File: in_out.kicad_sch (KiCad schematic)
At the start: 22 parts, among them J2 Conn_01x10, J3 Micro_SD_Card_Det1, SW1 SW_Push, SW2 SW_Push, U6 DM-OLED096-636

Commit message: modify ios
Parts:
- removed R19, R20: R_Small, Resistor_SMD:R_0603_1608Metric, symbol Device:R_Small
- added Q3: NMOS, Package_TO_SOT_SMD:SOT-23, symbol Transistor_FET:Q_NMOS_GSD
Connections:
- net IO3_EXT is gone; now on net IO40_EXT: J2.6 (Pin_6), R16.2
- net IO46 is gone; now on net IO39_EXT: D5.1 (TVS1)
- net IO9_EXT is gone; now on net IO41_EXT: J2.5 (Pin_5), R17.2
- net +3V3: now also BZ1.1 (+), R23.1, R24.1, R25.1
- net BUZZER: now also Q3.1 (G); no longer BZ1.1 (+)
- net GND: now also Q3.2 (S); no longer BZ1.2 (-), D7.2 (BK), D7.4 (GK), D7.6 (RK)
- net RGB_B: now also D7.2 (BK); no longer R23.1
- net RGB_G: now also D7.4 (GK); no longer R24.1
- net RGB_R: now also D7.6 (RK); no longer R25.1
- net IO0: no longer names the net of D6.3 (TVS2)
- net IO0: no longer R15.1
- net IO0_EXT renamed IO39_EXT
- net IO14 renamed IO41_EXT
- net IO41_EXT: no longer R18.1
- net IO14_EXT renamed IO42_EXT
- net IO42_EXT: now also D5.6 (TVS4)
- net IO3: no longer names the net of D6.1 (TVS1)
- net IO3: no longer R16.1
- net IO38 renamed IO40_EXT
- net IO38_EXT: no longer names the net of J2.3 (Pin_3)
- net IO46_EXT: no longer names the net of J2.2 (Pin_2)
- net IO9 renamed IO41
- net IO41: no longer D5.6 (TVS4)
- new net: BZ1.2 (-), Q3.3 (D)
- new net IO39: R15.1
- new net IO40: R16.1
- new net IO42: R18.1
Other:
- moved on the sheet: BZ1, D7, R23, R24, R25

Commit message: update pcb and schematic
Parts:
- removed J2: Conn_01x10, Connector_PinSocket_2.54mm:PinSocket_1x10_P2.54mm_Horizontal, symbol Connector_Generic:Conn_01x10
- added J2: Conn_01x08, Connector_PinSocket_2.54mm:PinSocket_1x08_P2.54mm_Horizontal, symbol Connector_Generic:Conn_01x08
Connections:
- net +3V3: now also J2.1 (Pin_1)
- net GND: now also J2.8 (Pin_8)
- net IO39_EXT: now also J2.5 (Pin_5)
- net IO40_EXT: now also J2.4 (Pin_4)
- net IO41_EXT: now also J2.3 (Pin_3)
- net IO42_EXT: now also J2.2 (Pin_2)
- net RXD0_EXT: now also J2.7 (Pin_7)
- net TXD0_EXT: now also J2.6 (Pin_6)
- no-connect marks 0 -> 2
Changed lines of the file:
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@@
 		(color 0 0 0 0)
 	)
+	(no_connect
+		(at 125.73 113.03)
+	)
+	(no_connect
+		(at 128.27 113.03)
+	)
 	(wire
 		(pts
@@
 	(wire
 		(pts
-			(xy 128.27 110.49) (xy 128.27 113.03)
-		)
-		(stroke
-			(width 0)
-			(type default)
-		)
-	)
-	(wire
-		(pts
 			(xy 165.1 64.77) (xy 165.1 60.96)
 		)
@@
 	(wire
 		(pts
-			(xy 68.58 127) (xy 81.28 127)
+			(xy 67.31 123.19) (xy 80.01 123.19)
 		)
 		(stroke
@@
 	(wire
 		(pts
-			(xy 80.01 133.35) (xy 80.01 132.08)
+			(xy 78.74 129.54) (xy 78.74 128.27)
 		)
 		(stroke
@@
 	(wire
 		(pts
-			(xy 68.58 121.92) (xy 81.28 121.92)
+			(xy 67.31 118.11) (xy 80.01 118.11)
 		)
 		(stroke
@@
 	(wire
 		(pts
-			(xy 68.58 116.84) (xy 81.28 116.84)
-		)
-		(stroke
-			(width 0)
-			(type default)
-		)
-	)
-	(wire
-		(pts
-			(xy 68.58 129.54) (xy 81.28 129.54)
+			(xy 67.31 113.03) (xy 80.01 113.03)
+		)
+		(stroke
+			(width 0)
+			(type default)
+		)
+	)
+	(wire
+		(pts
+			(xy 67.31 125.73) (xy 80.01 125.73)
 		)
 		(stroke
@@
 	(wire
 		(pts
-			(xy 125.73 110.49) (xy 125.73 113.03)
-		)
-		(stroke
-			(width 0)
-			(type default)
-		)
-	)
-	(wire
-		(pts
-			(xy 80.01 107.95) (xy 80.01 109.22)
+			(xy 78.74 109.22) (xy 78.74 110.49)
 		)
 		(stroke
@@
 	(wire
 		(pts
-			(xy 80.01 132.08) (xy 81.28 132.08)
+			(xy 78.74 128.27) (xy 80.01 128.27)
 		)
 		(stroke
@@
 	(wire
 		(pts
-			(xy 68.58 119.38) (xy 81.28 119.38)
+			(xy 67.31 115.57) (xy 80.01 115.57)
 		)
 		(stroke
@@
 	(wire
 		(pts
-			(xy 68.58 124.46) (xy 81.28 124.46)
+			(xy 67.31 120.65) (xy 80.01 120.65)
 		)
 		(stroke
@@
 	(wire
 		(pts
-			(xy 80.01 109.22) (xy 81.28 109.22)
+			(xy 78.74 110.49) (xy 80.01 110.49)
 		)
 		(stroke
@@
 	)
 	(label "TXD0_EXT"
-		(at 68.58 127 0)
+		(at 67.31 123.19 0)
 		(effects
 			(font
@@
 	)
 	(label "IO40_EXT"
-		(at 68.58 121.92 0)
+		(at 67.31 118.11 0)
 		(effects
 			(font
@@
 	)
 	(label "IO42_EXT"
-		(at 68.58 116.84 0)
+		(at 67.31 113.03 0)
 		(effects
 			(font
@@
 	)
 	(label "RXD0_EXT"
-		(at 68.58 129.54 0)
+		(at 67.31 125.73 0)
 		(effects
 			(font
@@
 	)
 	(label "IO41_EXT"
-		(at 68.58 119.38 0)
+		(at 67.31 115.57 0)
 		(effects
 			(font
@@
 	)
 	(label "IO39_EXT"
-		(at 68.58 124.46 0)
+		(at 67.31 120.65 0)
 		(effects
 			(font
@@
 			)
 			(justify left)
-		)
-	)
-	(symbol
-		(lib_id "Connector_Generic:Conn_01x10")
-		(at 86.36 119.38 0)
-		(unit 1)
-		(exclude_from_sim no)
-		(in_bom yes)
-		(on_board yes)
-		(dnp no)
-		(property "Reference" "J2"
-			(at 92.202 116.078 90)
-			(effects
-				(font
-					(size 1.27 1.27)
-				)
-				(justify right)
-			)
-		)
-		(property "Value" "Conn_01x10"
-			(at 89.662 116.078 90)
-			(effects
-				(font
-					(size 1.27 1.27)
-				)
-				(justify right)
-			)
-		)
-		(property "Footprint" "Connector_PinSocket_2.54mm:PinSocket_1x10_P2.54mm_Horizontal"
-			(at 86.36 119.38 0)
-			(effects
-				(font
-					(size 1.27 1.27)
-				)
-				(hide yes)
-			)
-		)
-		(property "Datasheet" "~"
-			(at 86.36 119.38 0)
-			(effects
-				(font
-					(size 1.27 1.27)
-				)
-				(hide yes)
-			)
-		)
-		(property "Description" "Generic connector, single row, 01x10, script generated (kicad-library-utils/schlib/autogen/connector/)"
-			(at 86.36 119.38 0)
-			(effects
-				(font
-					(size 1.27 1.27)
-				)
-				(hide yes)
-			)
-		)
-		(pin "6"
-		)
-		(pin "5"
-		)
-		(pin "7"
-		)
-		(pin "4"
-		)
-		(pin "3"
-		)
-		(pin "2"
-		)
-		(pin "1"
-		)
-		(pin "10"
-		)
-		(pin "8"
-		)
-		(pin "9"
-		)
-		(instances
-			(project ""
-				(path "/3130e1f2-bde1-4b12-bd54-0e1e50bd36da/1a9a8b3a-0ac6-451f-bc78-9d7f4c721b98"
-					(reference "J2")
-					(unit 1)
-				)
-			)
 		)
 	)
@@
 	)
 	(symbol
+		(lib_id "Connector_Generic:Conn_01x08")
+		(at 85.09 118.11 0)
+		(unit 1)
+		(exclude_from_sim no)
+		(in_bom yes)
+		(on_board yes)
+		(dnp no)
+		(property "Reference" "J2"
+			(at 90.932 113.284 90)
+			(effects
+				(font
+					(size 1.27 1.27)
+				)
+				(justify right)
+			)
+		)
+		(property "Value" "Conn_01x08"
+			(at 88.392 113.284 90)
+			(effects
+				(font
+					(size 1.27 1.27)
+				)
+				(justify right)
+			)
+		)
+		(property "Footprint" "Connector_PinSocket_2.54mm:PinSocket_1x08_P2.54mm_Horizontal"
+			(at 85.09 118.11 0)
+			(effects
+				(font
+					(size 1.27 1.27)
+				)
+				(hide yes)
+			)
+		)
+		(property "Datasheet" "~"
+			(at 85.09 118.11 0)
+			(effects
+				(font
+					(size 1.27 1.27)
+				)
+				(hide yes)
+			)
+		)
+		(property "Description" "Generic connector, single row, 01x08, script generated (kicad-library-utils/schlib/autogen/connector/)"
+			(at 85.09 118.11 0)
+			(effects
+				(font
+					(size 1.27 1.27)
+				)
+				(hide yes)
+			)
+		)
+		(pin "1"
+		)
+		(pin "6"
+		)
+		(pin "7"
+		)
+		(pin "4"
+		)
+		(pin "5"
+		)
+		(pin "8"
+		)
+		(pin "2"
+		)
+		(pin "3"
+		)
+		(instances
+			(project ""
+				(path "/3130e1f2-bde1-4b12-bd54-0e1e50bd36da/1a9a8b3a-0ac6-451f-bc78-9d7f4c721b98"
+					(reference "J2")
+					(unit 1)
+				)
+			)
+		)
+	)
+	(symbol
 		(lib_id "Device:R")
 		(at 170.18 64.77 90)
@@
 	(symbol
 		(lib_id "power:+3V3")
-		(at 80.01 107.95 0)
+		(at 78.74 109.22 0)
 		(unit 1)
 		(exclude_from_sim no)
@@
 		(dnp no)
 		(property "Reference" "#PWR031"
-			(at 80.01 111.76 0)
+			(at 78.74 113.03 0)
 			(effects
 				(font
@@
 		)
 		(property "Value" "+3V3"
-			(at 79.502 104.14 0)
+			(at 78.232 105.41 0)
 			(effects
 				(font
@@
 		)
 		(property "Footprint" ""
-			(at 80.01 107.95 0)
+			(at 78.74 109.22 0)
 			(effects
 				(font
@@
 		)
 		(property "Datasheet" ""
-			(at 80.01 107.95 0)
+			(at 78.74 109.22 0)
 			(effects
 				(font
@@
 		)
 		(property "Description" "Power symbol creates a global label with name \"+3V3\""
-			(at 80.01 107.95 0)
+			(at 78.74 109.22 0)
 			(effects
 				(font
@@
 	(symbol
 		(lib_id "power:GND")
-		(at 80.01 133.35 0)
+		(at 78.74 129.54 0)
 		(unit 1)
 		(exclude_from_sim no)
@@
 		(dnp no)
 		(property "Reference" "#PWR032"
-			(at 80.01 139.7 0)
+			(at 78.74 135.89 0)
 			(effects
 				(font
@@
 		)
 		(property "Value" "GND"
-			(at 80.01 137.414 0)
+			(at 78.74 133.604 0)
 			(effects
 				(font
@@
 		)
 		(property "Footprint" ""
-			(at 80.01 133.35 0)
+			(at 78.74 129.54 0)
 			(effects
 				(font
@@
 		)
 		(property "Datasheet" ""
-			(at 80.01 133.35 0)
+			(at 78.74 129.54 0)
 			(effects
 				(font
@@
 		)
 		(property "Description" "Power symbol creates a global label with name \"GND\" , ground"
-			(at 80.01 133.35 0)
-			(effects
-				(font
+			(at 78.74 129.54 0)
+			(effects
+				(font

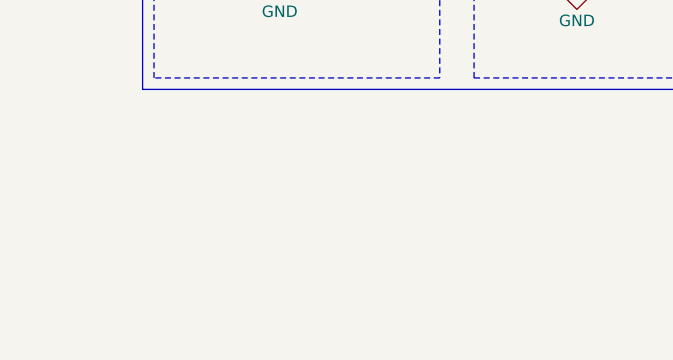
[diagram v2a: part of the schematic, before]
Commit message: Add encoder to schematic
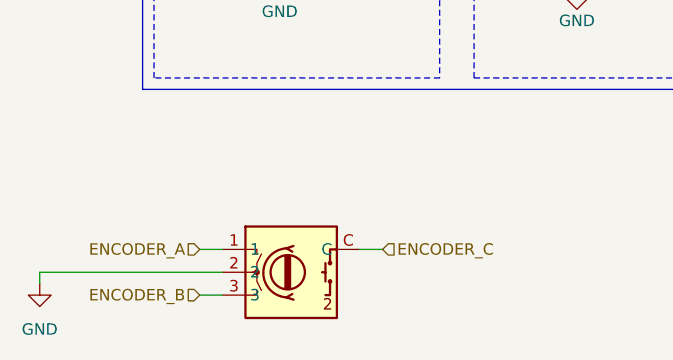
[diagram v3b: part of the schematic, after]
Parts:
- added U8: ~, Encoder:encoder, symbol encoder:encoder
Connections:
- net GND: now also U8.2
- new net ENCODER_A: U8.1
- new net ENCODER_B: U8.3
- new net ENCODER_C: U8.C
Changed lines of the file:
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@@
+	(wire
+		(pts
+			(xy 90.17 160.02) (xy 87.63 160.02)
+		)
+		(stroke
+			(width 0)
+			(type default)
+		)
+	)
 	(wire
 		(pts
@@
 	(wire
 		(pts
+			(xy 52.07 162.56) (xy 72.39 162.56)
+		)
+		(stroke
+			(width 0)
+			(type default)
+		)
+	)
+	(wire
+		(pts
 			(xy 212.09 67.31) (xy 213.36 67.31)
 		)
@@
 	(wire
 		(pts
+			(xy 52.07 163.83) (xy 52.07 162.56)
+		)
+		(stroke
+			(width 0)
+			(type default)
+		)
+	)
+	(wire
+		(pts
 			(xy 163.83 64.77) (xy 165.1 64.77)
 		)
@@
 	(wire
 		(pts
+			(xy 69.85 165.1) (xy 72.39 165.1)
+		)
+		(stroke
+			(width 0)
+			(type default)
+		)
+	)
+	(wire
+		(pts
 			(xy 212.09 80.01) (xy 213.36 80.01)
 		)
@@
 		(pts
 			(xy 67.31 120.65) (xy 80.01 120.65)
+		)
+		(stroke
+			(width 0)
+			(type default)
+		)
+	)
+	(wire
+		(pts
+			(xy 69.85 160.02) (xy 72.39 160.02)
 		)
 		(stroke
@@
 		(shape input)
 		(at 213.36 106.68 0)
+		(effects
+			(font
+				(size 1.27 1.27)
+			)
+			(justify left)
+		)
+	)
+	(hierarchical_label "ENCODER_B"
+		(shape input)
+		(at 69.85 165.1 180)
+		(effects
+			(font
+				(size 1.27 1.27)
+			)
+			(justify right)
+		)
+	)
+	(hierarchical_label "ENCODER_A"
+		(shape input)
+		(at 69.85 160.02 180)
+		(effects
+			(font
+				(size 1.27 1.27)
+			)
+			(justify right)
+		)
+	)
+	(hierarchical_label "ENCODER_C"
+		(shape input)
+		(at 90.17 160.02 0)
 		(effects
 			(font
@@
 				(path "/3130e1f2-bde1-4b12-bd54-0e1e50bd36da/1a9a8b3a-0ac6-451f-bc78-9d7f4c721b98"
 					(reference "R24")
+					(unit 1)
+				)
+			)
+		)
+	)
+	(symbol
+		(lib_id "power:GND")
+		(at 52.07 163.83 0)
+		(unit 1)
+		(exclude_from_sim no)
+		(in_bom yes)
+		(on_board yes)
+		(dnp no)
+		(fields_autoplaced yes)
+		(property "Reference" "#PWR047"
+			(at 52.07 170.18 0)
+			(effects
+				(font
+					(size 1.27 1.27)
+				)
+				(hide yes)
+			)
+		)
+		(property "Value" "GND"
+			(at 52.07 168.91 0)
+			(effects
+				(font
+					(size 1.27 1.27)
+				)
+			)
+		)
+		(property "Footprint" ""
+			(at 52.07 163.83 0)
+			(effects
+				(font
+					(size 1.27 1.27)
+				)
+				(hide yes)
+			)
+		)
+		(property "Datasheet" ""
+			(at 52.07 163.83 0)
+			(effects
+				(font
+					(size 1.27 1.27)
+				)
+				(hide yes)
+			)
+		)
+		(property "Description" "Power symbol creates a global label with name \"GND\" , ground"
+			(at 52.07 163.83 0)
+			(effects
+				(font
+					(size 1.27 1.27)
+				)
+				(hide yes)
+			)
+		)
+		(pin "1"
+		)
+		(instances
+			(project ""
+				(path "/3130e1f2-bde1-4b12-bd54-0e1e50bd36da/1a9a8b3a-0ac6-451f-bc78-9d7f4c721b98"
+					(reference "#PWR047")
 					(unit 1)
 				)
@@
 					(unit 1)
 				)
+			)
+		)
+	)
+	(symbol
+		(lib_id "encoder:encoder")
+		(at 80.01 162.56 0)
+		(unit 1)
+		(exclude_from_sim no)
+		(in_bom yes)
+		(on_board yes)
+		(dnp no)
+		(fields_autoplaced yes)
+		(property "Reference" "U8"
+			(at 80.01 162.56 0)
+			(effects
+				(font
+					(size 1.27 1.27)
+				)
+				(hide yes)
+			)
+		)
+		(property "Value" "~"
+			(at 80.01 154.94 0)
+			(effects
+				(font
+					(size 1.27 1.27)
+				)
+			)
+		)
+		(property "Footprint" "Encoder:encoder"
+			(at 80.01 162.56 0)
+			(effects
+				(font
+					(size 1.27 1.27)
+				)
+				(hide yes)
+			)
+		)
+		(property "Datasheet" ""
+			(at 80.01 162.56 0)
+			(effects
+				(font
+					(size 1.27 1.27)
+				)
+				(hide yes)
+			)
+		)
+		(property "Description" ""
+			(at 80.01 162.56 0)
+			(effects
+				(font
+					(size 1.27 1.27)
+				)
+				(hide yes)
+			)
+		)
+		(pin "C"
+		)
+		(pin "3"
+		)
+		(pin "2"
+		)
+		(pin "1"
+		)
+		(instances
+			(project ""
+				(path "/3130e1f2-bde1-4b12-bd54-0e1e50bd36da/1a9a8b3a-0ac6-451f-bc78-9d7f4c721b98"
+					(reference "U8")
+					(unit 1)
+				)

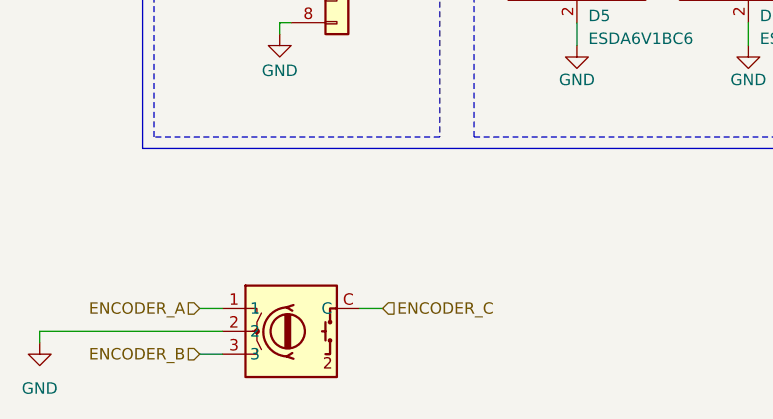
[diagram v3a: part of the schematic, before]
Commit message: Fix encoder schematic
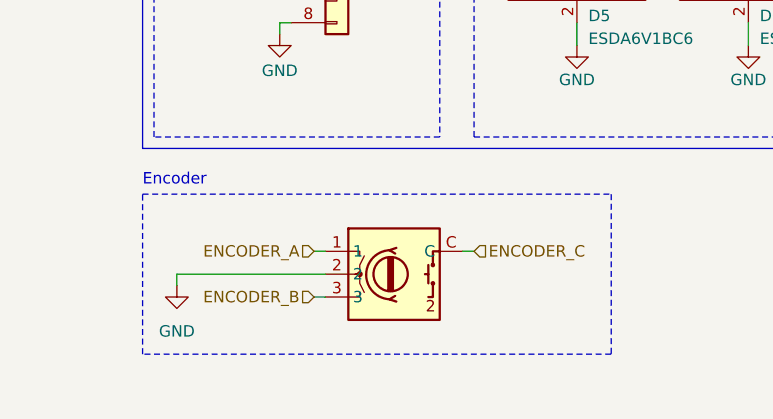
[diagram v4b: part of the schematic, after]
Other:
- note added: "Encoder"
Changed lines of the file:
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@@
+	)
+	(rectangle
+		(start 63.5 147.32)
+		(end 115.57 165.1)
+		(stroke
+			(width 0)
+			(type dash)
+		)
+		(fill
+			(type none)
+		)
 	)
 	(rectangle
@@
 		(exclude_from_sim no)
 		(at 75.438 99.06 0)
+		(effects
+			(font
+				(size 1.27 1.27)
+			)
+		)
+	)
+	(text "Encoder"
+		(exclude_from_sim no)
+		(at 67.056 145.796 0)
 		(effects
 			(font
@@
 	(wire
 		(pts
-			(xy 90.17 160.02) (xy 87.63 160.02)
+			(xy 100.33 153.67) (xy 99.06 153.67)
 		)
 		(stroke
@@
 	(wire
 		(pts
-			(xy 52.07 162.56) (xy 72.39 162.56)
+			(xy 67.31 156.21) (xy 83.82 156.21)
 		)
 		(stroke
@@
 	(wire
 		(pts
-			(xy 52.07 163.83) (xy 52.07 162.56)
+			(xy 67.31 157.48) (xy 67.31 156.21)
 		)
 		(stroke
@@
 	(wire
 		(pts
-			(xy 69.85 165.1) (xy 72.39 165.1)
+			(xy 82.55 158.75) (xy 83.82 158.75)
 		)
 		(stroke
@@
 	(wire
 		(pts
-			(xy 69.85 160.02) (xy 72.39 160.02)
+			(xy 82.55 153.67) (xy 83.82 153.67)
 		)
 		(stroke
@@
 	(hierarchical_label "ENCODER_B"
 		(shape input)
-		(at 69.85 165.1 180)
+		(at 82.55 158.75 180)
 		(effects
 			(font
@@
 	(hierarchical_label "ENCODER_A"
 		(shape input)
-		(at 69.85 160.02 180)
+		(at 82.55 153.67 180)
 		(effects
 			(font
@@
 	(hierarchical_label "ENCODER_C"
 		(shape input)
-		(at 90.17 160.02 0)
+		(at 100.33 153.67 0)
 		(effects
 			(font
@@
 	(symbol
 		(lib_id "power:GND")
-		(at 52.07 163.83 0)
+		(at 67.31 157.48 0)
 		(unit 1)
 		(exclude_from_sim no)
@@
 		(fields_autoplaced yes)
 		(property "Reference" "#PWR047"
-			(at 52.07 170.18 0)
+			(at 67.31 163.83 0)
 			(effects
 				(font
@@
 		)
 		(property "Value" "GND"
-			(at 52.07 168.91 0)
+			(at 67.31 162.56 0)
 			(effects
 				(font
@@
 		)
 		(property "Footprint" ""
-			(at 52.07 163.83 0)
+			(at 67.31 157.48 0)
 			(effects
 				(font
@@
 		)
 		(property "Datasheet" ""
-			(at 52.07 163.83 0)
+			(at 67.31 157.48 0)
 			(effects
 				(font
@@
 		)
 		(property "Description" "Power symbol creates a global label with name \"GND\" , ground"
-			(at 52.07 163.83 0)
+			(at 67.31 157.48 0)
 			(effects
 				(font
@@
 	(symbol
 		(lib_id "encoder:encoder")
-		(at 80.01 162.56 0)
+		(at 91.44 156.21 0)
 		(unit 1)
 		(exclude_from_sim no)
@@
 		(fields_autoplaced yes)
 		(property "Reference" "U8"
-			(at 80.01 162.56 0)
+			(at 91.44 156.21 0)
 			(effects
 				(font
@@
 		)
 		(property "Value" "~"
-			(at 80.01 154.94 0)
+			(at 91.44 148.59 0)
 			(effects
 				(font
@@
 		)
 		(property "Footprint" "Encoder:encoder"
-			(at 80.01 162.56 0)
+			(at 91.44 156.21 0)
 			(effects
 				(font
@@
 		)
 		(property "Datasheet" ""
-			(at 80.01 162.56 0)
+			(at 91.44 156.21 0)
 			(effects
 				(font
@@
 		)
 		(property "Description" ""
-			(at 80.01 162.56 0)
-			(effects
-				(font
+			(at 91.44 156.21 0)
+			(effects
+				(font

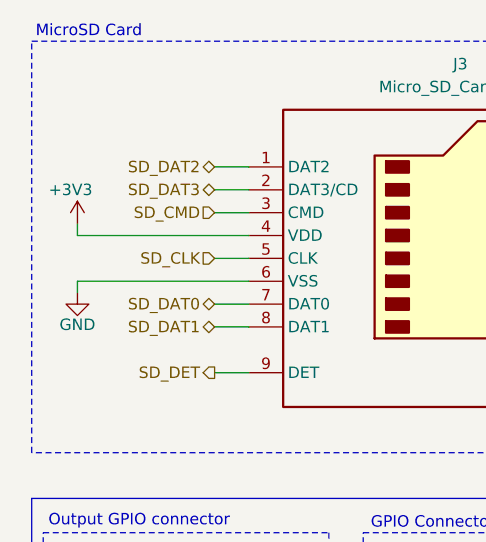
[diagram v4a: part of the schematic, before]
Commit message: Add bypass capacitors
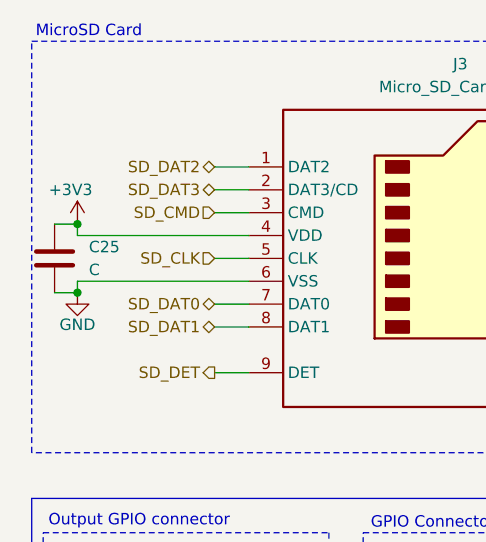
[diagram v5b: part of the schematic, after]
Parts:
- added C25: C, Capacitor_SMD:C_0805_2012Metric, symbol Device:C
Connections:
- net +3V3: now also C25.1
- net GND: now also C25.2
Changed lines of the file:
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@@
 	)
 	(junction
+		(at 68.58 66.04)
+		(diameter 0)
+		(color 0 0 0 0)
+	)
+	(junction
 		(at 165.1 83.82)
 		(diameter 0)
@@
 	)
 	(junction
+		(at 68.58 73.66)
+		(diameter 0)
+		(color 0 0 0 0)
+	)
+	(junction
 		(at 165.1 64.77)
 		(diameter 0)
@@
 	(wire
 		(pts
+			(xy 66.04 73.66) (xy 68.58 73.66)
+		)
+		(stroke
+			(width 0)
+			(type default)
+		)
+	)
+	(wire
+		(pts
 			(xy 190.5 111.76) (xy 190.5 106.68)
 		)
@@
 	(wire
 		(pts
+			(xy 66.04 66.04) (xy 68.58 66.04)
+		)
+		(stroke
+			(width 0)
+			(type default)
+		)
+	)
+	(wire
+		(pts
 			(xy 154.94 119.38) (xy 157.48 119.38)
 		)
@@
 					(unit 1)
 				)
+			)
+		)
+	)
+	(symbol
+		(lib_id "Device:C")
+		(at 66.04 69.85 0)
+		(unit 1)
+		(exclude_from_sim no)
+		(in_bom yes)
+		(on_board yes)
+		(dnp no)
+		(fields_autoplaced yes)
+		(property "Reference" "C25"
+			(at 69.85 68.5799 0)
+			(effects
+				(font
+					(size 1.27 1.27)
+				)
+				(justify left)
+			)
+		)
+		(property "Value" "C"
+			(at 69.85 71.1199 0)
+			(effects
+				(font
+					(size 1.27 1.27)
+				)
+				(justify left)
+			)
+		)
+		(property "Footprint" "Capacitor_SMD:C_0805_2012Metric"
+			(at 67.0052 73.66 0)
+			(effects
+				(font
+					(size 1.27 1.27)
+				)
+				(hide yes)
+			)
+		)
+		(property "Datasheet" "~"
+			(at 66.04 69.85 0)
+			(effects
+				(font
+					(size 1.27 1.27)
+				)
+				(hide yes)
+			)
+		)
+		(property "Description" "Unpolarized capacitor"
+			(at 66.04 69.85 0)
+			(effects
+				(font
+					(size 1.27 1.27)
+				)
+				(hide yes)
+			)
+		)
+		(pin "2"
+		)
+		(pin "1"
+		)
+		(instances
+			(project "pipu-zero"
+				(path "/3130e1f2-bde1-4b12-bd54-0e1e50bd36da/1a9a8b3a-0ac6-451f-bc78-9d7f4c721b98"
+					(reference "C25")
+					(unit 1)
+				)
